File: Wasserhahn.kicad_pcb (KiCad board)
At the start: 2 copper layers, 76.2 x 78.1 mm, 18 parts, among them J1 Mains, J2 Ball_Valve_Contacts, J3 ToRelais, J4 PRGM_ADAPTER, J5 Boot/PRGM, U1 ESP-WROOM-02

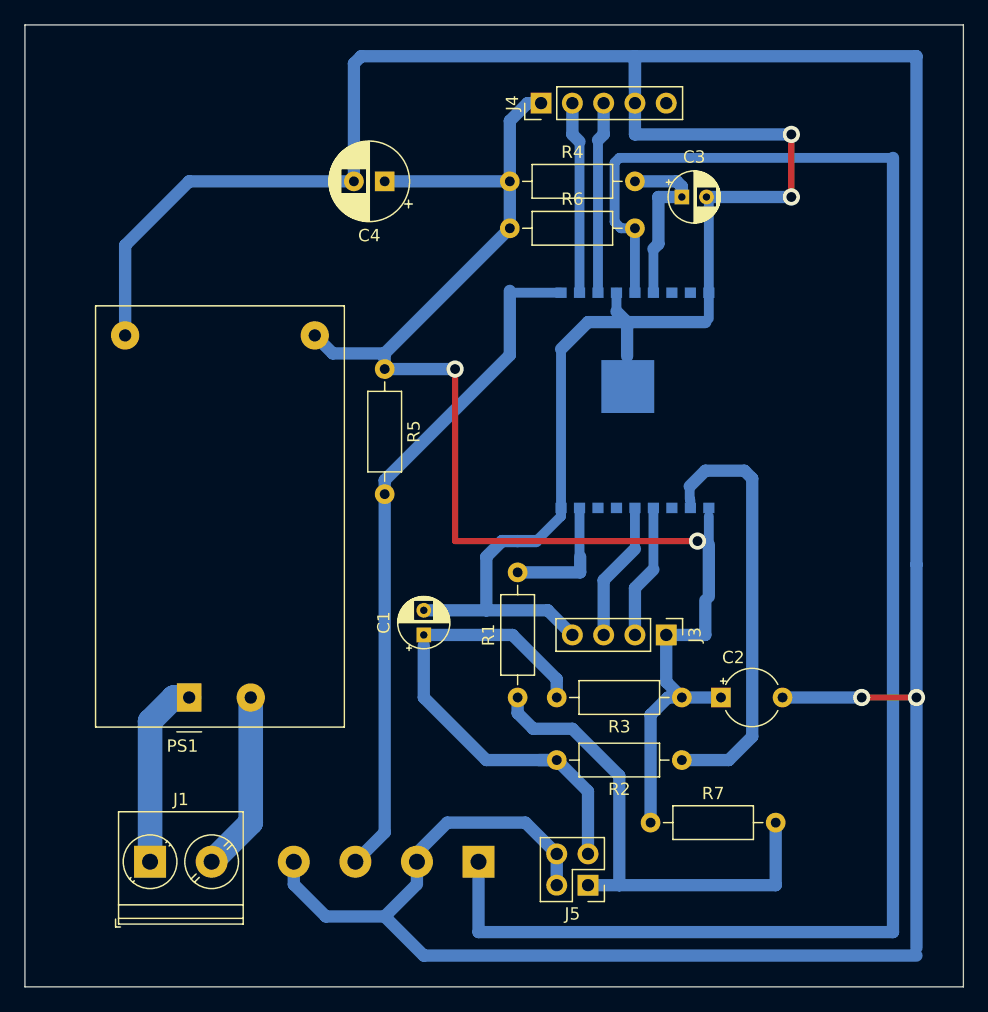
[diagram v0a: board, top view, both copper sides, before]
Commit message: added connections for IO2, removed short circuit, swaped EN and RST on Jumper
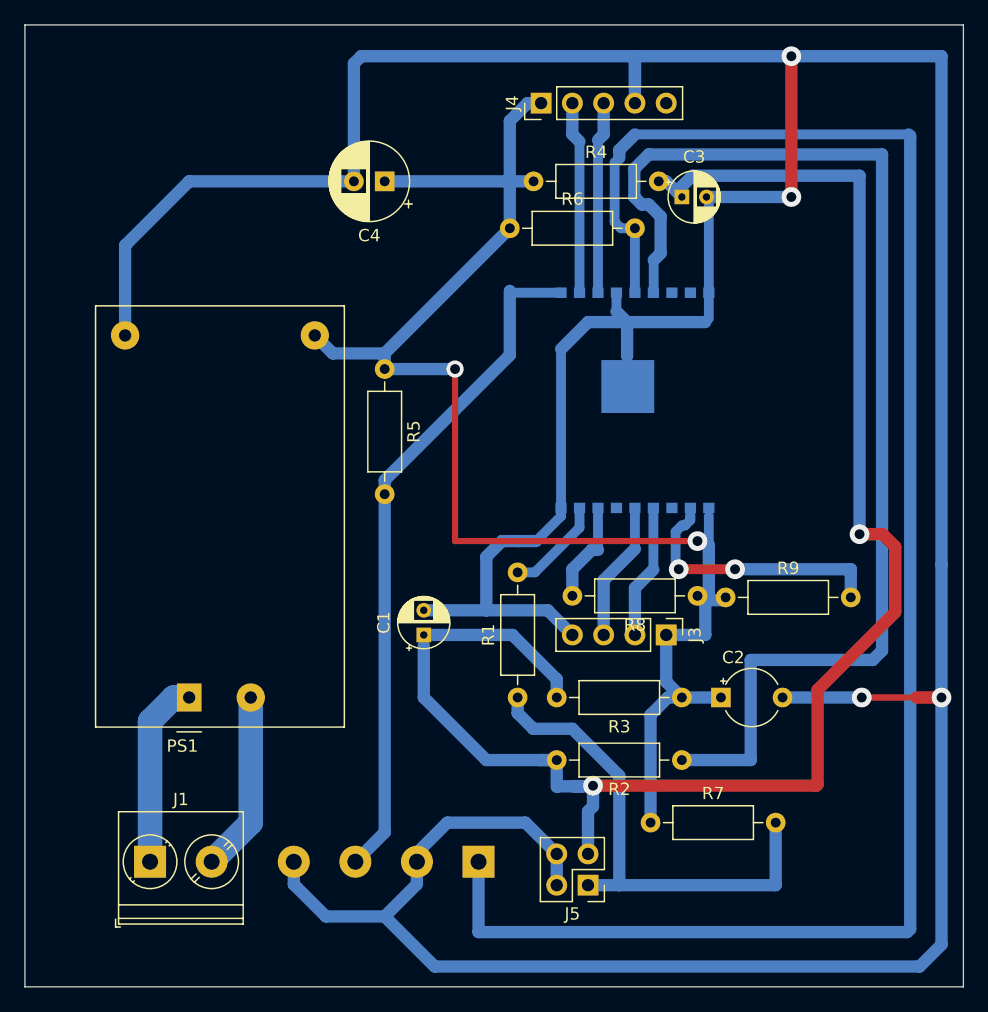
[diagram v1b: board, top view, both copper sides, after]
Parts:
- added R8: 10K, Resistor_THT:R_Axial_DIN0207_L6.3mm_D2.5mm_P10.16mm_Horizontal, F.Cu at (165.1, 74.3)
- added R9: 10K, Resistor_THT:R_Axial_DIN0207_L6.3mm_D2.5mm_P10.16mm_Horizontal, F.Cu at (167.4, 74.4)
- moved R4 1.93 mm to (151.8, 40.6)
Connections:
- C1 pad 1: Net-(C1-Pad1) -> Net-(C3-Pad1)
- J5 pad 3: Net-(C1-Pad1) -> Net-(C3-Pad1)
- R2 pad 2: Net-(C1-Pad1) -> Net-(C3-Pad1)
- R3 pad 2: Net-(C1-Pad1) -> Net-(C3-Pad1)
- U1 pad 15: Net-(C3-Pad1) -> Net-(R2-Pad1)
- U1 pad 2: Net-(R2-Pad1) -> Net-(R9-Pad2)
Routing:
- net Net-(C3-Pad1): track 14.7 -> 135.2 mm, vias 0 -> 2
- net Net-(R2-Pad1): track 35.1 -> 97.1 mm
- net Net-(C1-Pad1): track 41.9 -> 0.00 mm
- net Net-(R9-Pad2): track 0.00 -> 21.6 mm, vias 0 -> 3
- net Net-(R8-Pad2): track 0.00 -> 7.95 mm
- net /Input_Open: track 136.9 -> 142.5 mm
- net /VCC3V3: track 118.6 -> 123.1 mm
- net /GND: track 353.0 -> 350.7 mm
- net Net-(R1-Pad2): track 10.3 -> 8.13 mm

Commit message: GPIO15 pulled low, jumper to disconnect Power for flashing
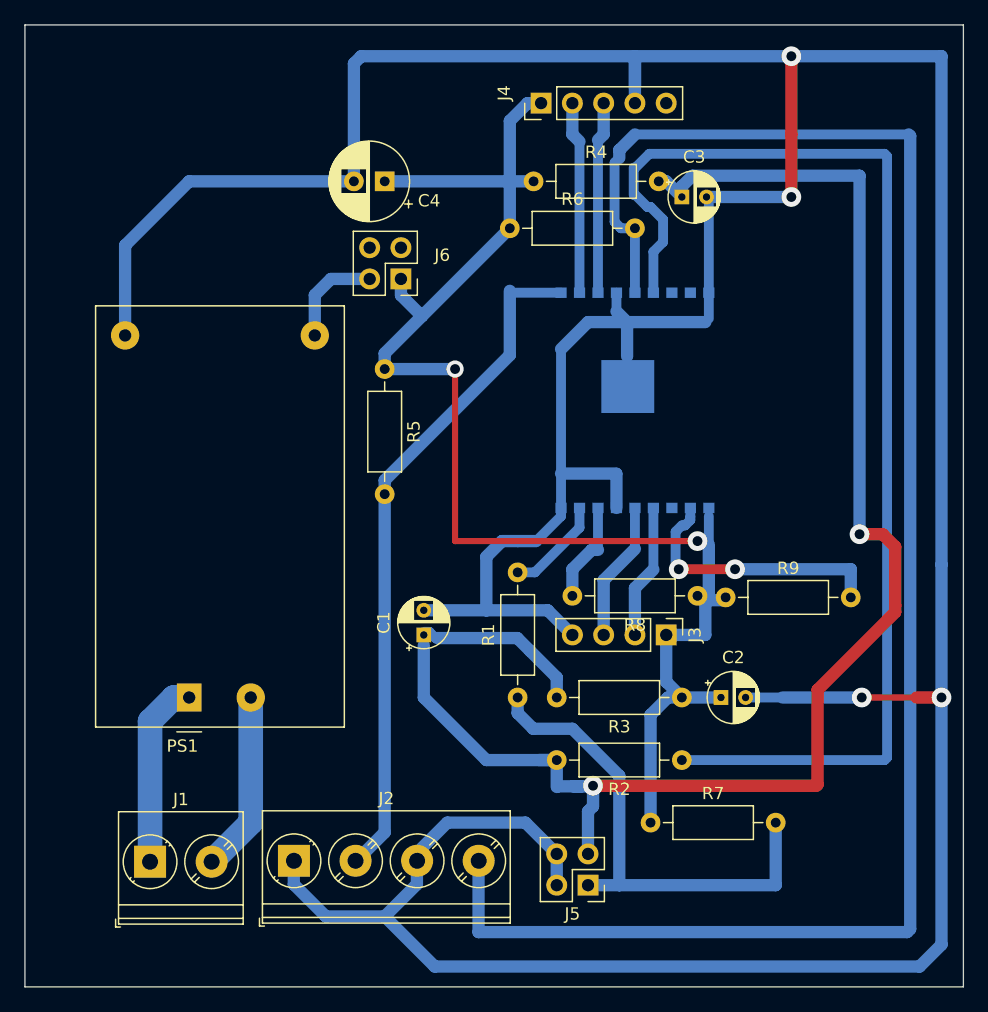
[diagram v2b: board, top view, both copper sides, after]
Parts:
- added J6: Isolate, Connector_PinHeader_2.54mm:PinHeader_2x02_P2.54mm_Vertical, F.Cu at (141.0, 48.6)
- C2: footprint Capacitor_THT:CP_Radial_Tantal_D4.5mm_P5.00mm -> Capacitor_THT:CP_Radial_D4.0mm_P2.00mm
- J2: moved to F.Cu
- J5: value Boot/PRGM -> RST/PRGM
- moved J2 15.0 mm to (132.3, 95.8), turned to 0 degrees
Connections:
- C1 pad 1: Net-(C3-Pad1) -> Net-(C1-Pad1)
- PS1 pad 4: /VCC3V3 -> Net-(J6-Pad2)
- R3 pad 2: Net-(C3-Pad1) -> Net-(C1-Pad1)
- U1 pad 6: Net-(U1-Pad6) -> /GND
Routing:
- net Net-(C3-Pad1): track 135.2 -> 120.5 mm
- net Net-(C1-Pad1): track 0.00 -> 14.0 mm
- net /GND: track 350.7 -> 360.9 mm
- net Net-(J6-Pad2): track 0.00 -> 8.28 mm
- net /VCC3V3: track 123.1 -> 120.5 mm
- net Net-(R2-Pad1): track 97.1 -> 98.1 mm
